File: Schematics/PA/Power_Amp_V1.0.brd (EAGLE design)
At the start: 50.5 x 76.8 mm, 102 parts, among them J1 4_PIN_AMPCONN, J12 1725724, J13 1725724, J14 1725724, J2 1984633, J3 2TERMINAL_SPEAKER, J4 2TERMINAL_SPEAKER, J5 2TERMINAL_SPEAKER, U1 LME49830, U2 LME49830, U3 LME49830

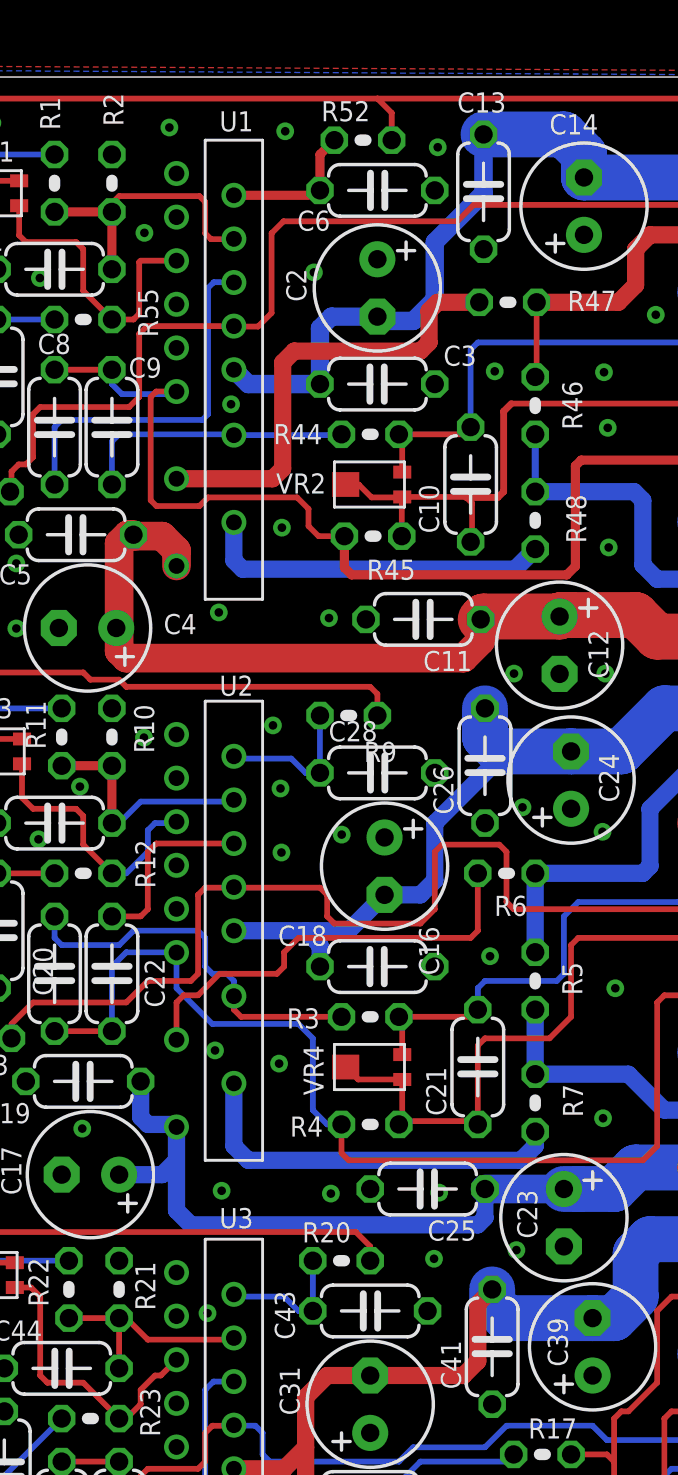
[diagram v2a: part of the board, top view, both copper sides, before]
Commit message: changes footprint on mute cap
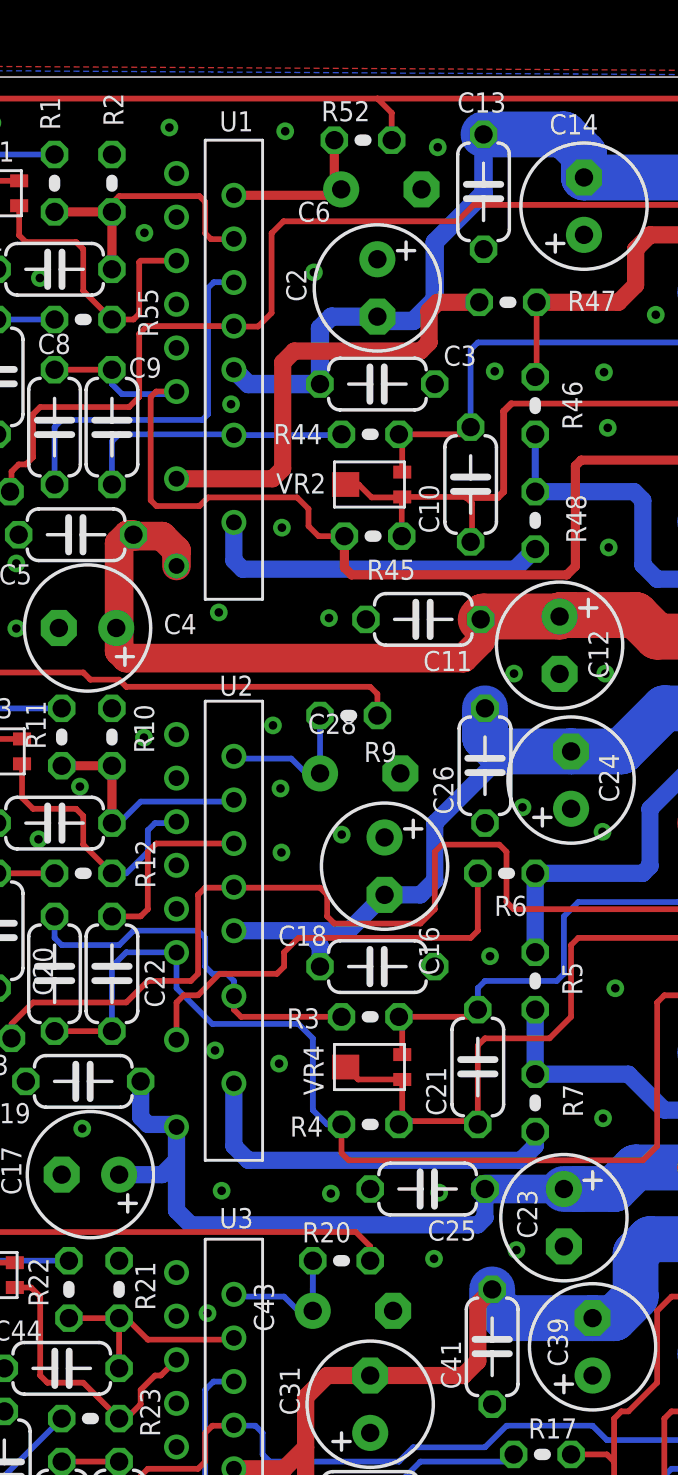
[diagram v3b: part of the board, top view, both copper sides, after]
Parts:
- C28, C6: value 100uF -> 1000uF; device rcl:C050-024X044 -> Amplifier_Parts:8MM_CAP_BSILK
- C43: device rcl:C050-024X044 -> Amplifier_Parts:8MM_CAP_BSILK
- moved C43 0.99 mm to (19.1, 22.6)
- moved C28 0.98 mm to (19.4, 46.4)
- moved C6 0.39 mm to (20.3, 72.2)
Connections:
- net GND: now also C28.-1, C43.-1, C6.-1; no longer C28.2, C43.2, C6.2
- net N$14: now also C28.+1; no longer C28.1
- net N$37: now also C43.+1; no longer C43.1
- net N$85: now also C6.+1; no longer C6.1
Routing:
- net N$85: track 6.39 -> 8.06 mm
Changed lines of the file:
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@@
 <attribute name="VALUE" x="48.387" y="29.2735" size="1.27" layer="27" ratio="10" rot="R90"/>
 </element>
-<element name="C28" library="rcl" package="C050-024X044" value="100uF" x="20.32" y="46.0375" smashed="yes">
-<attribute name="NAME" x="18.161" y="47.4345" size="0.889" layer="25" font="vector" ratio="15"/>
-<attribute name="VALUE" x="18.161" y="43.3705" size="1.27" layer="27" ratio="10"/>
+<element name="C28" library="Amplifier_Parts" package="8MM_CAP_BSILK" value="1000uF" x="19.401140625" y="46.365534375" smashed="yes">
+<attribute name="NAME" x="17.242140625" y="47.762534375" size="0.889" layer="25" font="vector" ratio="15"/>
+<attribute name="VALUE" x="17.242140625" y="43.698534375" size="1.27" layer="27" ratio="10"/>
 </element>
 <element name="C29" library="rcl" package="C050-024X044" value="22pF" x="6.0325" y="43.815" smashed="yes">
@@
 <attribute name="VALUE" x="48.387" y="6.882584375" size="1.27" layer="27" ratio="10" rot="R90"/>
 </element>
-<element name="C43" library="rcl" package="C050-024X044" value="100uF" x="20.0025" y="22.225" smashed="yes">
-<attribute name="NAME" x="16.66963125" y="20.9537875" size="0.889" layer="25" font="vector" ratio="15" rot="R90"/>
-<attribute name="VALUE" x="17.8435" y="19.558" size="1.27" layer="27" ratio="10"/>
+<element name="C43" library="Amplifier_Parts" package="8MM_CAP_BSILK" value="100uF" x="19.07718125" y="22.5793125" smashed="yes">
+<attribute name="NAME" x="15.7443125" y="21.3081" size="0.889" layer="25" font="vector" ratio="15" rot="R90"/>
+<attribute name="VALUE" x="16.91818125" y="19.9123125" size="1.27" layer="27" ratio="10"/>
 </element>
 <element name="C44" library="rcl" package="C050-024X044" value="0.1uF" x="6.35" y="19.685" smashed="yes">
@@
 <attribute name="VALUE" x="9.144" y="59.2455" size="1.27" layer="27" ratio="10" rot="R180"/>
 </element>
-<element name="C6" library="rcl" package="C050-024X044" value="100uF" x="20.32" y="71.8185" smashed="yes">
-<attribute name="NAME" x="16.7715" y="70.032396875" size="0.889" layer="25" font="vector" ratio="15"/>
-<attribute name="VALUE" x="18.161" y="69.1515" size="1.27" layer="27" ratio="10"/>
+<element name="C6" library="Amplifier_Parts" package="8MM_CAP_BSILK" value="1000uF" x="20.33640625" y="72.2121375" smashed="yes">
+<attribute name="NAME" x="16.78790625" y="70.426034375" size="0.889" layer="25" font="vector" ratio="15"/>
+<attribute name="VALUE" x="18.17740625" y="69.5451375" size="1.27" layer="27" ratio="10"/>
 </element>
 <element name="C7" library="rcl" package="C050-024X044" value="0.1uF" x="3.4925" y="63.5635" smashed="yes" rot="R90">
@@
 <signal name="N$85">
 <contactref element="R52" pad="2"/>
-<contactref element="C6" pad="1"/>
+<contactref element="C6" pad="+1"/>
 <contactref element="U1" pad="P2"/>
-<wire x1="13.97" y1="71.601" x2="17.5625" y2="71.601" width="0.4064" layer="1"/>
-<wire x1="17.5625" y1="71.601" x2="17.78" y2="71.8185" width="0.4064" layer="1"/>
-<wire x1="17.78" y1="71.8185" x2="17.78" y2="73.406" width="0.4064" layer="1"/>
-<wire x1="17.78" y1="73.406" x2="18.415" y2="74.041" width="0.4064" layer="1"/>
+<wire x1="13.97" y1="71.601" x2="18.702" y2="71.601" width="0.4064" layer="1"/>
+<wire x1="18.702" y1="71.601" x2="18.71840625" y2="71.8621375" width="0.4064" layer="1"/>
+<wire x1="18.71840625" y1="71.8621375" x2="18.415" y2="71.4685" width="0.4064" layer="1"/>
+<wire x1="18.415" y1="71.4685" x2="18.415" y2="74.041" width="0.4064" layer="1"/>
 </signal>
 <signal name="GND">
-<contactref element="C6" pad="2"/>
+<contactref element="C6" pad="-1"/>
 <contactref element="C15" pad="1"/>
 <contactref element="C14" pad="+"/>
@@
 <contactref element="C11" pad="2"/>
 <contactref element="J1" pad="4"/>
-<contactref element="C28" pad="2"/>
+<contactref element="C28" pad="-1"/>
 <contactref element="C27" pad="1"/>
 <contactref element="C24" pad="+"/>
@@
 <contactref element="C23" pad="-"/>
 <contactref element="C25" pad="2"/>
-<contactref element="C43" pad="2"/>
+<contactref element="C43" pad="-1"/>
 <contactref element="C42" pad="1"/>
 <contactref element="C39" pad="+"/>
@@
 <signal name="N$14">
 <contactref element="R9" pad="2"/>
-<contactref element="C28" pad="1"/>
+<contactref element="C28" pad="+1"/>
 <contactref element="U2" pad="P2"/>
-<wire x1="17.78" y1="48.5775" x2="17.78" y2="46.0375" width="0.254" layer="16"/>
-<wire x1="17.78" y1="46.0375" x2="17.145" y2="46.0375" width="0.254" layer="16"/>
+<wire x1="17.78" y1="48.5775" x2="17.783140625" y2="46.015534375" width="0.254" layer="16"/>
+<wire x1="17.783140625" y1="46.015534375" x2="17.145" y2="46.0375" width="0.254" layer="16"/>
 <wire x1="17.145" y1="46.0375" x2="16.51" y2="46.6725" width="0.254" layer="16"/>
 <wire x1="16.51" y1="46.6725" x2="14.07" y2="46.6725" width="0.254" layer="16"/>
@@
 <signal name="N$37">
 <contactref element="R20" pad="2"/>
-<contactref element="C43" pad="1"/>
+<contactref element="C43" pad="+1"/>
 <contactref element="U3" pad="P2"/>
-<wire x1="17.4625" y1="24.4475" x2="17.4625" y2="22.225" width="0.254" layer="16"/>
-<wire x1="17.4625" y1="22.225" x2="16.8275" y2="22.225" width="0.254" layer="16"/>
+<wire x1="17.4625" y1="24.4475" x2="17.45918125" y2="22.2293125" width="0.254" layer="16"/>
+<wire x1="17.45918125" y1="22.2293125" x2="16.8275" y2="22.225" width="0.254" layer="16"/>
 <wire x1="16.8275" y1="22.225" x2="16.1925" y2="22.86" width="0.254" layer="16"/>
 <wire x1="16.1925" y1="22.86" x2="14.07" y2="22.86" width="0.254" layer="16"/>

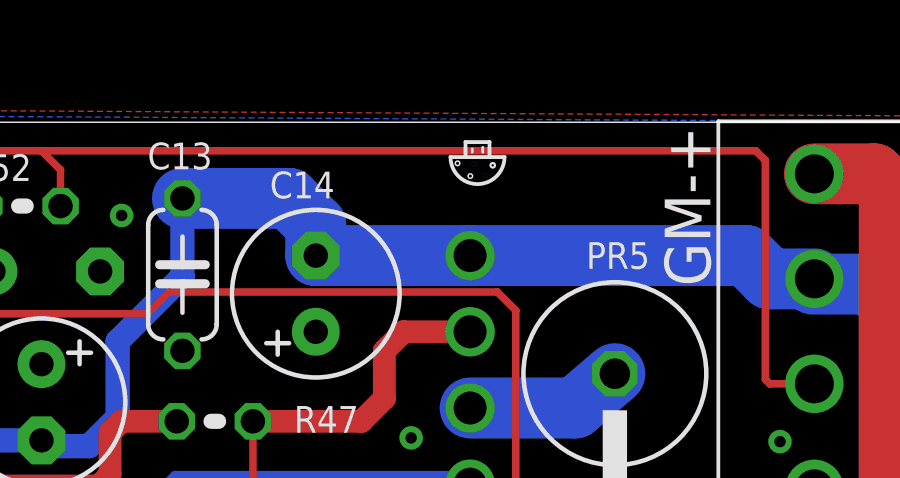
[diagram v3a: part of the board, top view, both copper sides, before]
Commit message: moved mushroom logo
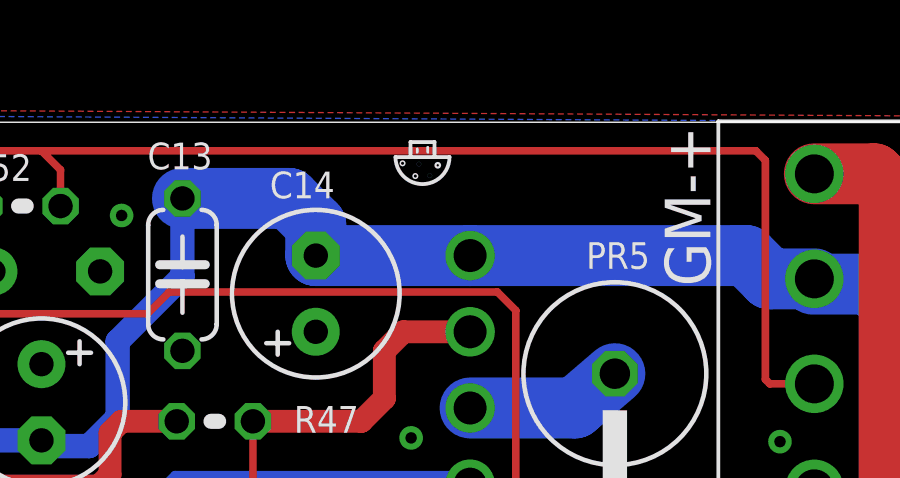
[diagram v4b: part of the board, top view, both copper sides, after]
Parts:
- moved U$17 1.83 mm to (33.0, 75.4)
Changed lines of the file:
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@@
 <?xml version="1.0" encoding="utf-8"?>
 <!DOCTYPE eagle SYSTEM "eagle.dtd">
-<eagle version="6.5.0">
+<eagle version="7.4.0">
 <drawing>
 <settings>
@@
 <setting verticaltext="up"/>
 </settings>
-<grid distance="0.003125" unitdist="mic" unit="inch" style="lines" multiple="1" display="yes" altdistance="0.025" altunitdist="inch" altunit="inch"/>
+<grid distance="0.0125" unitdist="inch" unit="inch" style="lines" multiple="1" display="yes" altdistance="0.025" altunitdist="inch" altunit="inch"/>
 <layers>
 <layer number="1" name="Top" color="4" fill="1" visible="yes" active="yes"/>
@@
 <pass name="Default">
 <param name="RoutingGrid" value="50mil"/>
+<param name="AutoGrid" value="1"/>
+<param name="Efforts" value="0"/>
+<param name="TopRouterVariant" value="1"/>
 <param name="tpViaShape" value="round"/>
 <param name="PrefDir.1" value="|"/>
@@
 <attribute name="NAME" x="40.435215625" y="5.917165625" size="0.889" layer="25" font="vector" ratio="15"/>
 </element>
-<element name="U$17" library="PersonalLogos" package="MUSHROOM" value="" x="34.854378125" y="75.410053125" rot="R180"/>
+<element name="U$17" library="PersonalLogos" package="MUSHROOM" value="" x="33.0208125" y="75.410053125" rot="R180"/>
 </elements>
 <signals>

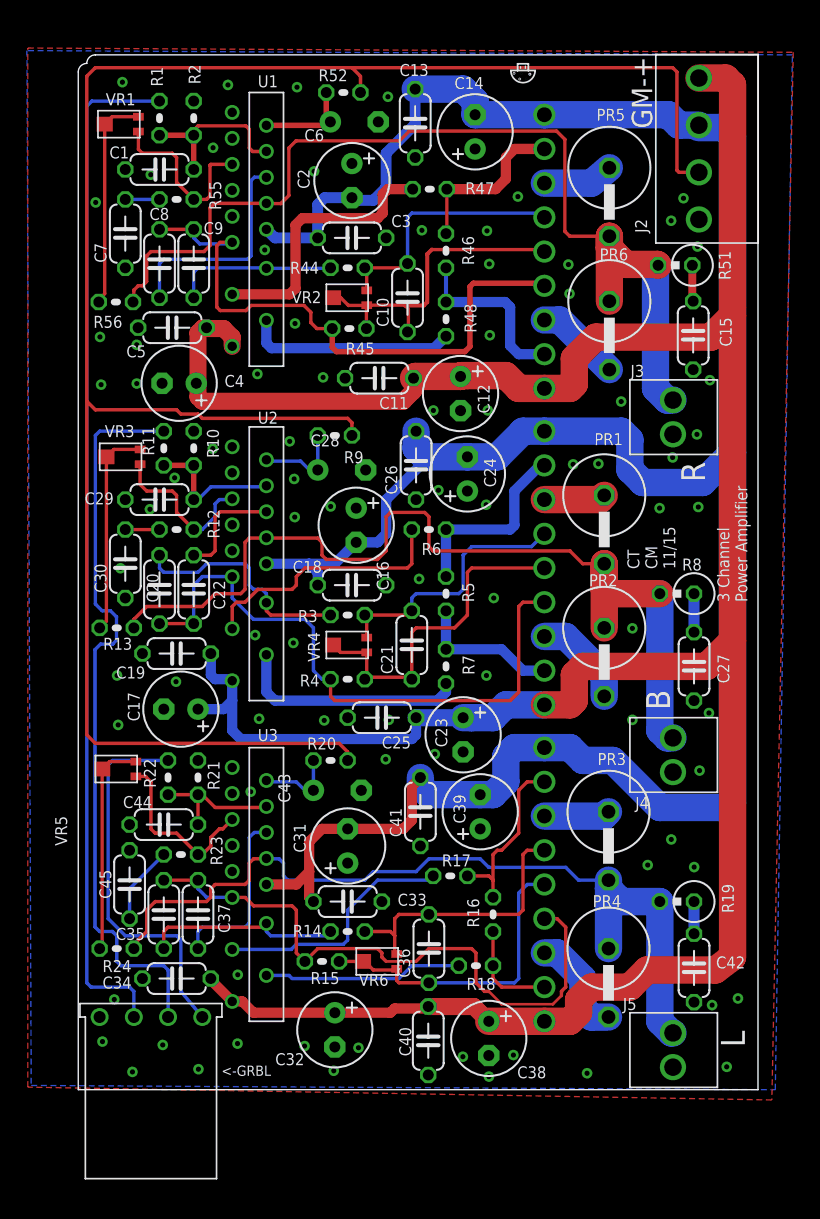
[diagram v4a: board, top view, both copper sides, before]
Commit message: updated PA
updated footprint for mute cap
added logo
changed silkscreen
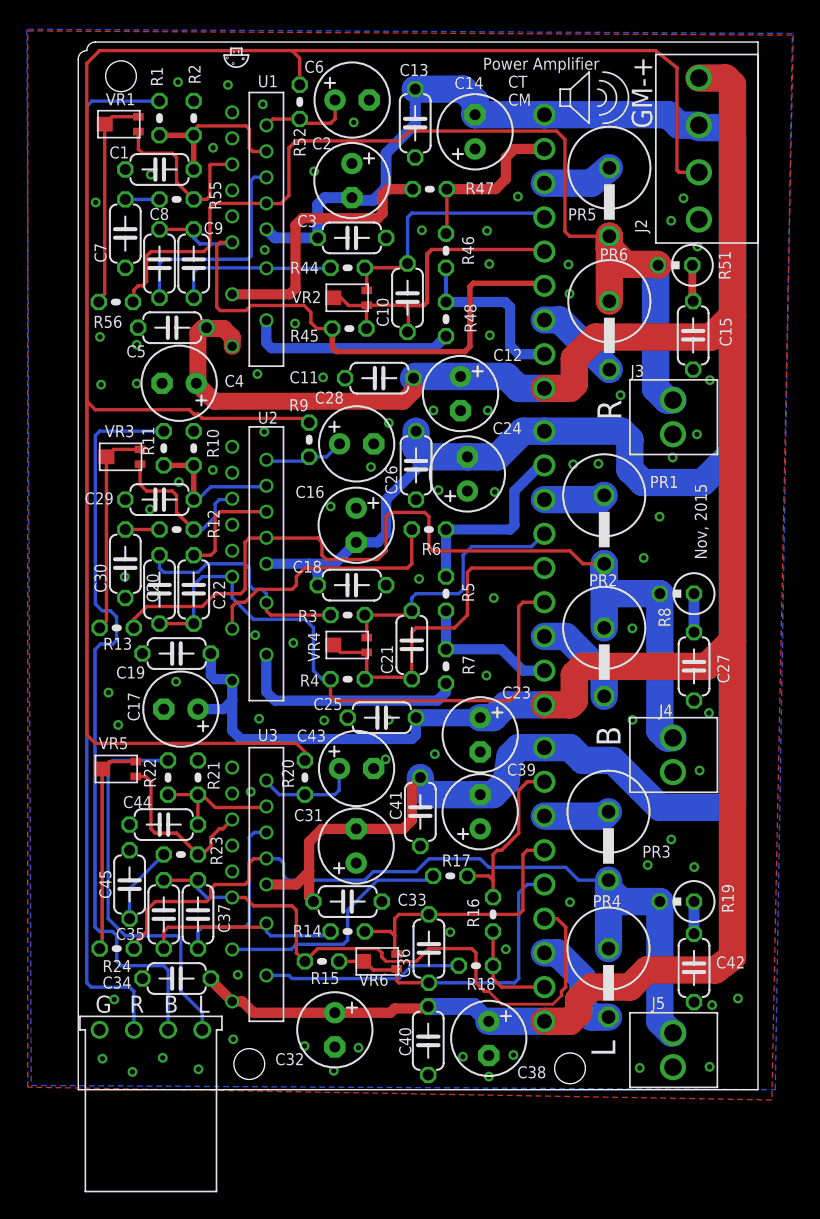
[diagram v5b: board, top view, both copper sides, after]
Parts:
- added U$48: (no value), PersonalLogos:SPEAKER
- C28, C6: value 1000uF -> 100uF; device Amplifier_Parts:8MM_CAP_BSILK -> rcl:E2,5-6
- C43: device Amplifier_Parts:8MM_CAP_BSILK -> rcl:E2,5-6
- moved U$17 21.3 mm to (11.7, 76.6)
- moved R52 3.31 mm to (16.4, 73.3), turned to 270 degrees
- moved R20 2.29 mm to (16.8, 23.2), turned to 270 degrees
- moved C43 2.03 mm to (20.7, 23.8)
- moved C28 2.03 mm to (20.7, 48.0)
- moved R9 1.93 mm to (17.1, 48.3), turned to 270 degrees
- moved C23 1.27 mm to (29.8, 26.4)
- moved C6 1.27 mm to (20.3, 73.5)
- moved J1 0.95 mm to (5.40, 4.45)
- moved C31 0.63 mm to (20.6, 18.1)
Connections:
- net GND: now also C28.-, C43.-, C6.-; no longer C28.-1, C43.-1, C6.-1
- net N$14: now also C28.+; no longer C28.+1
- net N$37: now also C43.+; no longer C43.+1
- net N$85: now also C6.+; no longer C6.+1
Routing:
- net V+: track 243.7 -> 228.5 mm
- net MUTE: track 146.0 -> 141.1 mm
- net N$37: track 6.01 -> 7.66 mm
- net N$85: track 8.06 -> 6.95 mm
- net LEFT_IN: track 28.4 -> 29.4 mm
- net RIGHT_IN: track 76.3 -> 77.3 mm
- net BASS_IN: track 55.3 -> 56.2 mm
- net N$14: track 6.68 -> 6.00 mm
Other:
- board size 50.5 x 76.8 mm -> 50.5 x 77.8 mm
- board text added: "CT CM"
- board text added: "G"
- board text added: "Nov, 2015"
- board text added: "Power Amplifier"
- board text removed: "3 Channel Power Amplifier"
- board text removed: "<-GRBL"
- board text removed: "CT CM 11/15"

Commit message: made small change to PA
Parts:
- moved J4 1.91 mm to (41.0, 29.5)
- moved C27 1.90 mm to (45.7, 33.3)
- moved R8 1.27 mm to (44.5, 38.1)
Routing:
- net V+: track 228.5 -> 229.7 mm
- net N$13: track 2.86 -> 2.22 mm
- net BASS_OUT: track 69.4 -> 68.9 mm
